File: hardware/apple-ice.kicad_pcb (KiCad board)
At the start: 2 copper layers, 100 x 77.7 mm, 83 parts, among them J1 TO_SP_DRIVE, J2 USB_B_Micro, J3 SPI_FLASH_PROG, J4 Conn_02x15_Odd_Even, P1 A2Bus-apple2, SW1 SW_Push, SW2 SW_Push, SW3 SW_Push, U1 SN74LVC8T245PW, U10 W25Q16JVSS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

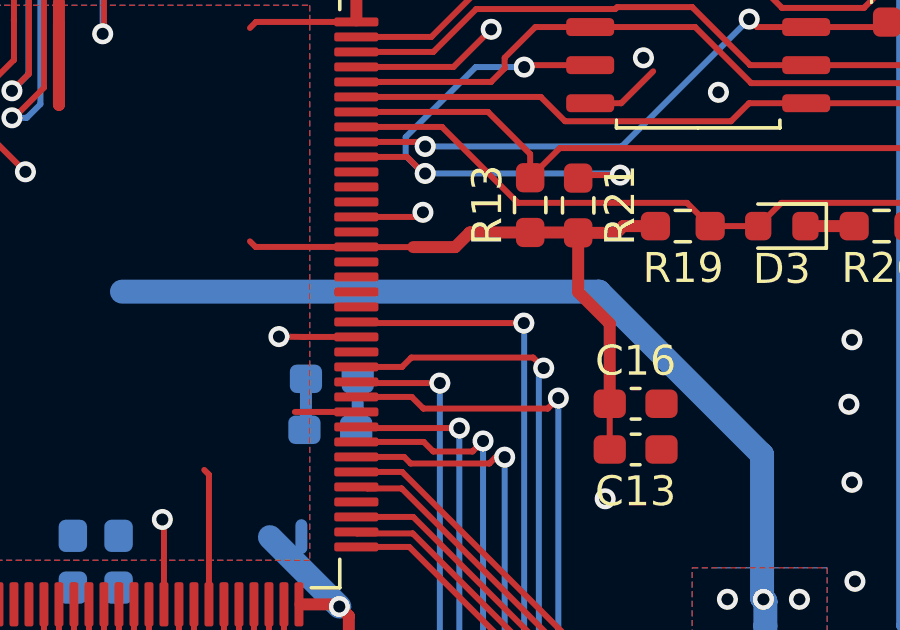
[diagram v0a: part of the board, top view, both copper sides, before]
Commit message: Move io_strobe signal to an FPGA pin that is not shared with the PLL
Signed-off-by: Rangel Ivanov <rangelivanov88@gmail.com>
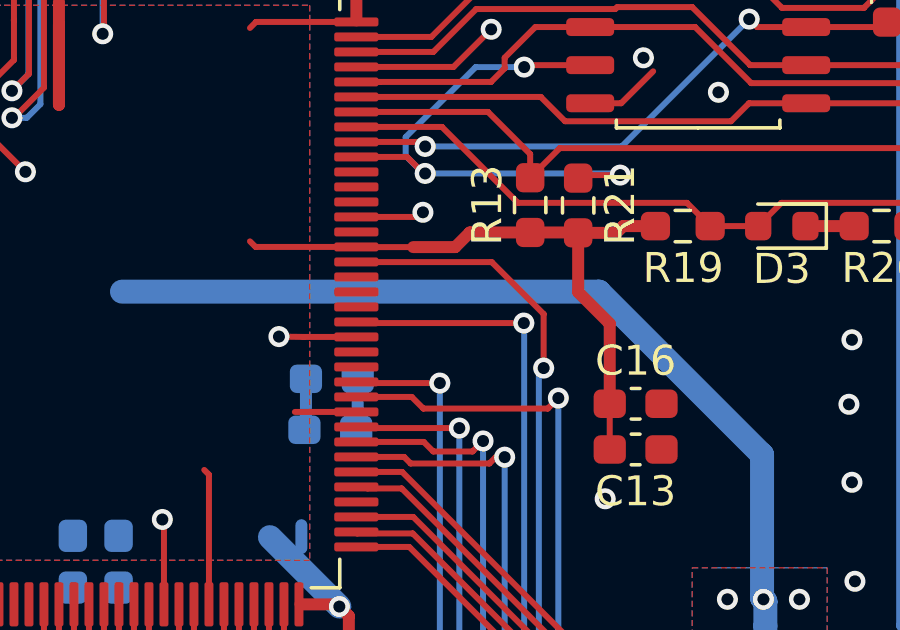
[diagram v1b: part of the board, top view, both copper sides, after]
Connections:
- U6 pad 49: /~IOSTROBE_33 -> Net-(U6-Pad49)
- U6 pad 56: Net-(U6-Pad56) -> /~IOSTROBE_33
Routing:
- net /~IOSTROBE_33: track 28.3 -> 30.6 mm

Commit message: Rev 0.2
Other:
- board text added: "Apple ][ iCE rev 0.2"
- board text removed: "Apple iCE rev 0.1"
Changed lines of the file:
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@@
     (effects (font (size 1 1) (thickness 0.15)))
   )
-  (gr_text "Apple iCE rev 0.1\n" (at 105.02 91.118) (layer F.SilkS)
+  (gr_text "Apple ][ iCE rev 0.2\n\n" (at 105.97 92.068) (layer F.SilkS)
     (effects (font (size 1.5 1.5) (thickness 0.15)))
   )
